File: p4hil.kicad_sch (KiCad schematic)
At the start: 7 parts, among them J14 Conn_01x04, SW1 SW_Push, SW2 SW_Push

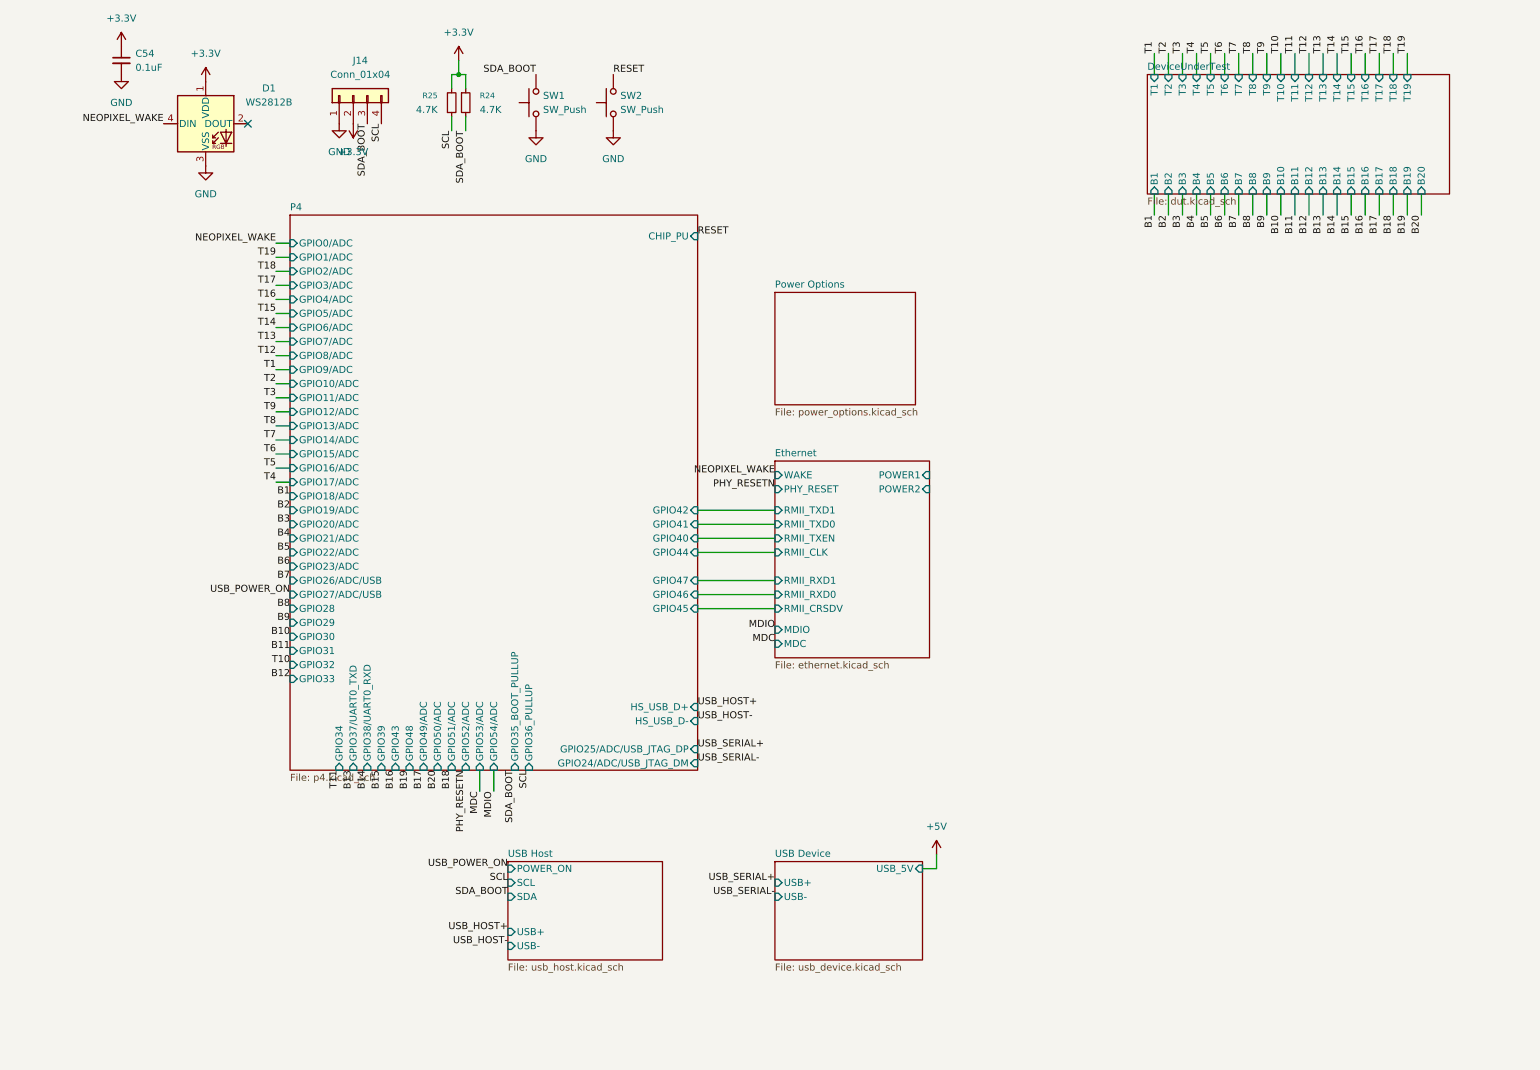
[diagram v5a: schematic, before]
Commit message: Add IO expanders, swap ethernet and move USB LEDs
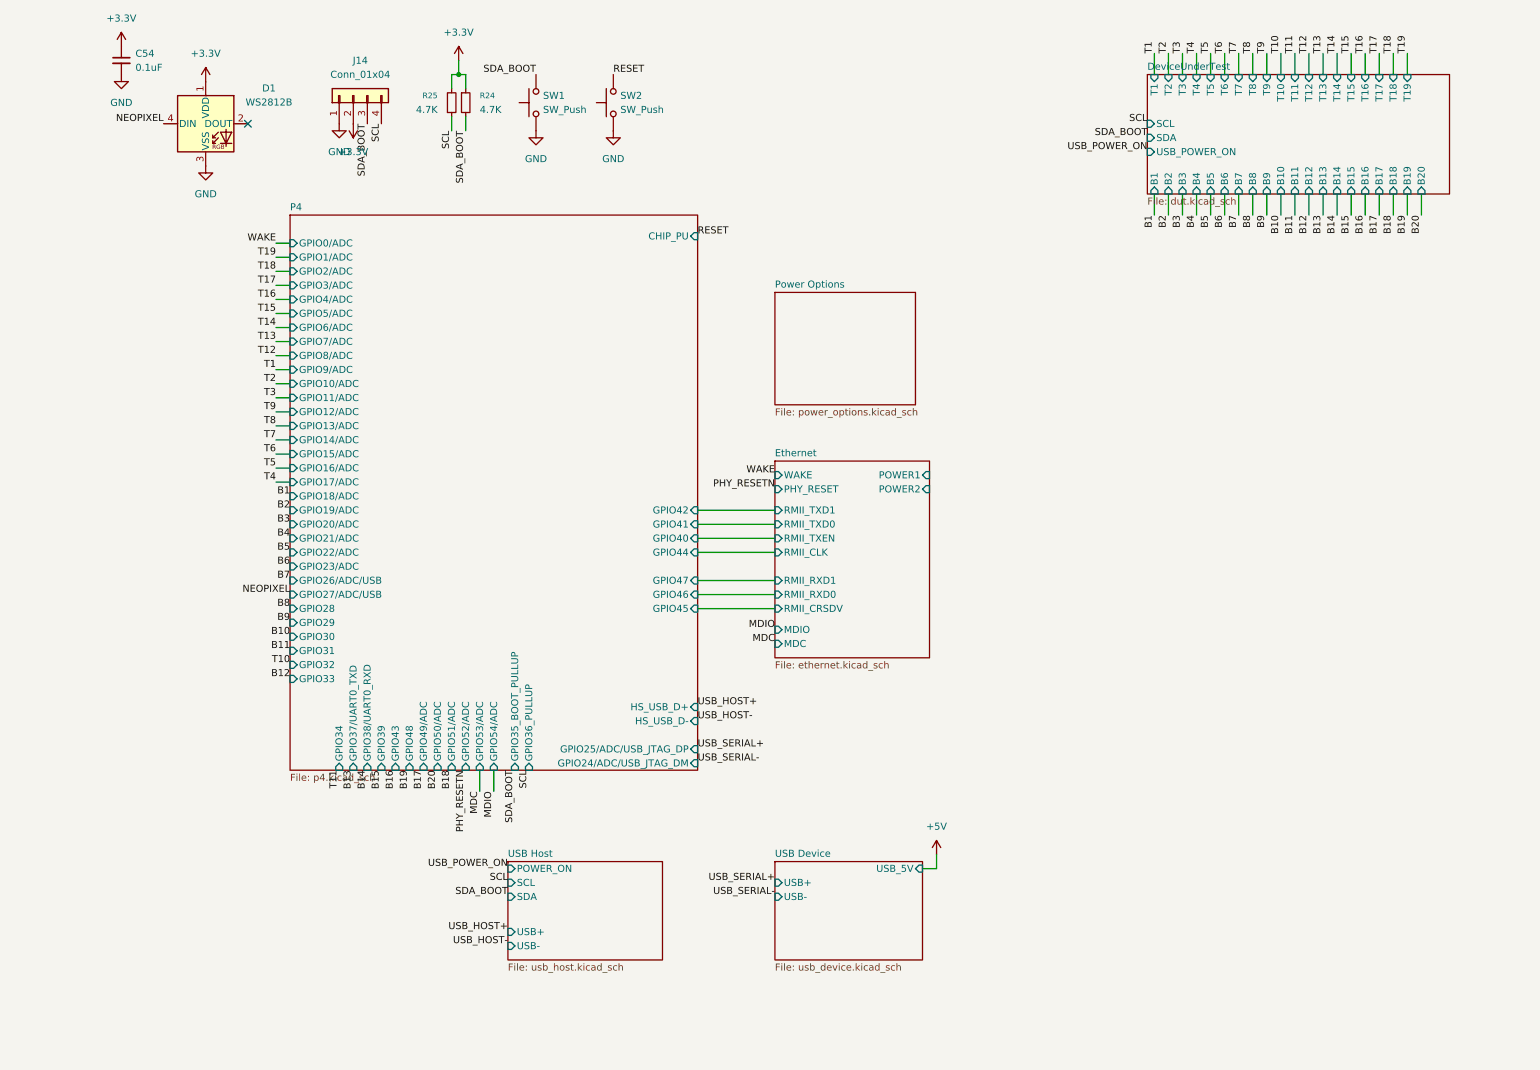
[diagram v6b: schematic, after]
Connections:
- net NEOPIXEL_WAKE renamed NEOPIXEL
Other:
- sheet DeviceUnderTest ports: added SCL, SDA, USB_POWER_ON; removed none
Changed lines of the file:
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@@
 		)
 	)
-	(label "NEOPIXEL_WAKE"
+	(label "USB_POWER_ON"
+		(at 208.28 39.37 180)
+		(effects
+			(font
+				(size 1.27 1.27)
+			)
+			(justify right bottom)
+		)
+	)
+	(label "WAKE"
 		(at 50.8 55.88 180)
 		(effects
@@
 		)
 	)
+	(label "SCL"
+		(at 208.28 34.29 180)
+		(effects
+			(font
+				(size 1.27 1.27)
+			)
+			(justify right bottom)
+		)
+	)
 	(label "T10"
 		(at 53.34 132.08 180)
@@
 		)
 	)
-	(label "NEOPIXEL_WAKE"
+	(label "WAKE"
 		(at 140.97 97.79 180)
 		(effects
@@
 		)
 	)
-	(label "B12"
-		(at 53.34 134.62 180)
+	(label "NEOPIXEL"
+		(at 53.34 119.38 180)
 		(effects
 			(font
@@
 		)
 	)
-	(label "USB_HOST+"
-		(at 127 139.7 0)
+	(label "B12"
+		(at 53.34 134.62 180)
 		(effects
 			(font
 				(size 1.27 1.27)
 			)
-			(justify left bottom)
+			(justify right bottom)
 		)
 	)
-	(label "USB_POWER_ON"
-		(at 53.34 119.38 180)
+	(label "USB_HOST+"
+		(at 127 139.7 0)
 		(effects
 			(font
 				(size 1.27 1.27)
 			)
-			(justify right bottom)
+			(justify left bottom)
 		)
 	)
@@
 		)
 	)
-	(label "NEOPIXEL_WAKE"
+	(label "NEOPIXEL"
 		(at 30.48 34.29 180)
 		(effects
@@
 	)
 	(label "SDA_BOOT"
+		(at 208.28 36.83 180)
+		(effects
+			(font
+				(size 1.27 1.27)
+			)
+			(justify right bottom)
+		)
+	)
+	(label "SDA_BOOT"
 		(at 67.31 34.29 270)
 		(effects
@@
 			)
 		)
+		(pin "SCL" input
+			(at 208.28 34.29 180)
+			(effects
+				(font
+					(size 1.27 1.27)
+				)
+				(justify left)
+			)
+		)
+		(pin "SDA" input
+			(at 208.28 36.83 180)
+			(effects
+				(font
+					(size 1.27 1.27)
+				)
+				(justify left)
+			)
+		)
+		(pin "USB_POWER_ON" input
+			(at 208.28 39.37 180)
+			(effects
+				(font
+					(size 1.27 1.27)
+				)
+				(justify left)
+			)
+		)
